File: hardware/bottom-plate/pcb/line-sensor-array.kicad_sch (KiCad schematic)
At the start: 1 part

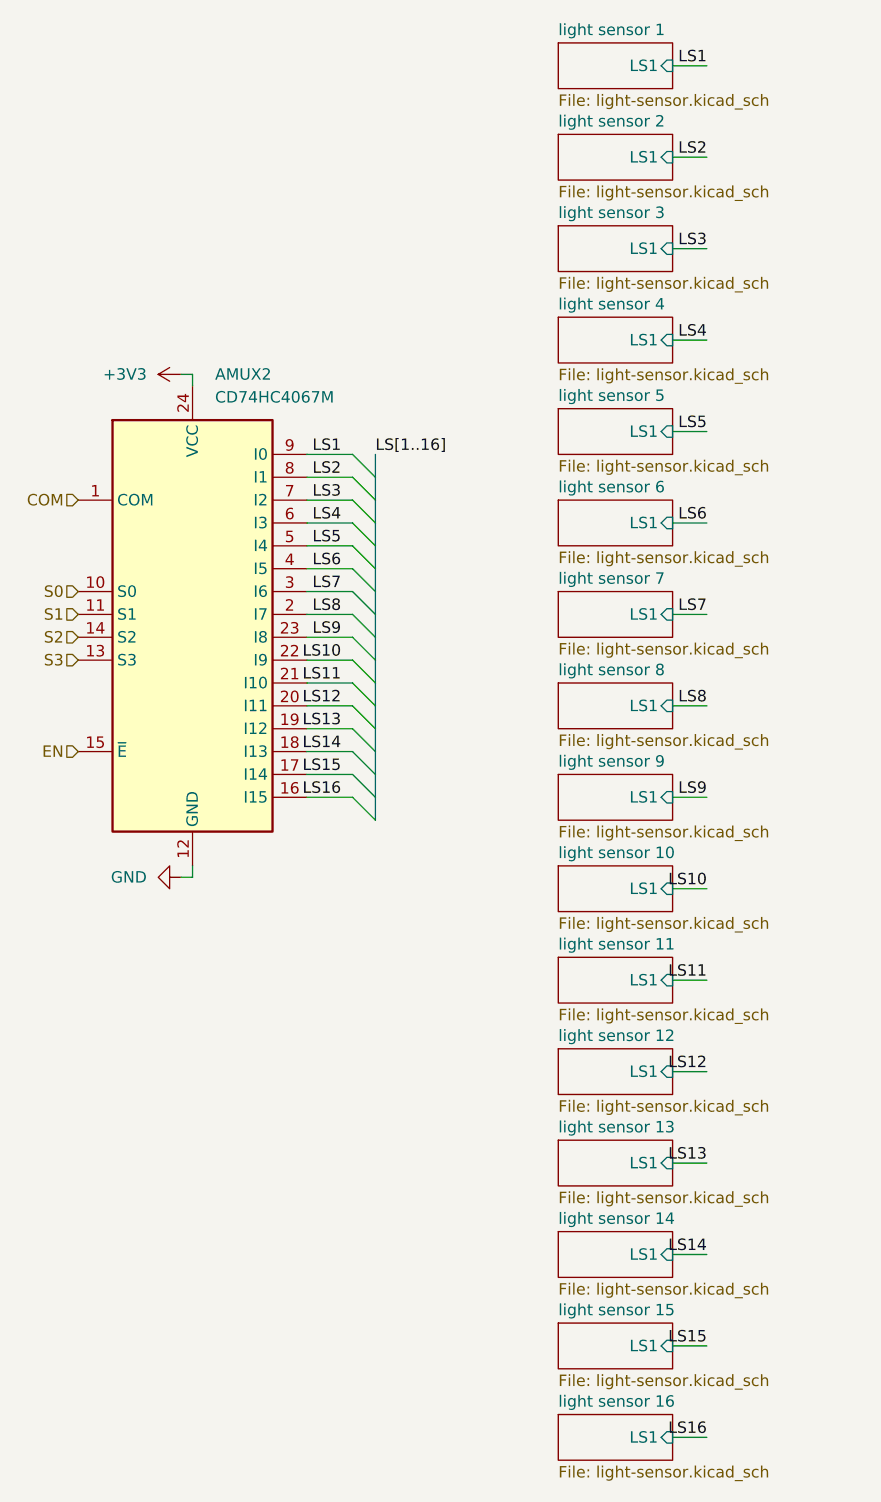
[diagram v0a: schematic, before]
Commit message: cleaned up bottom plate schematic numbering
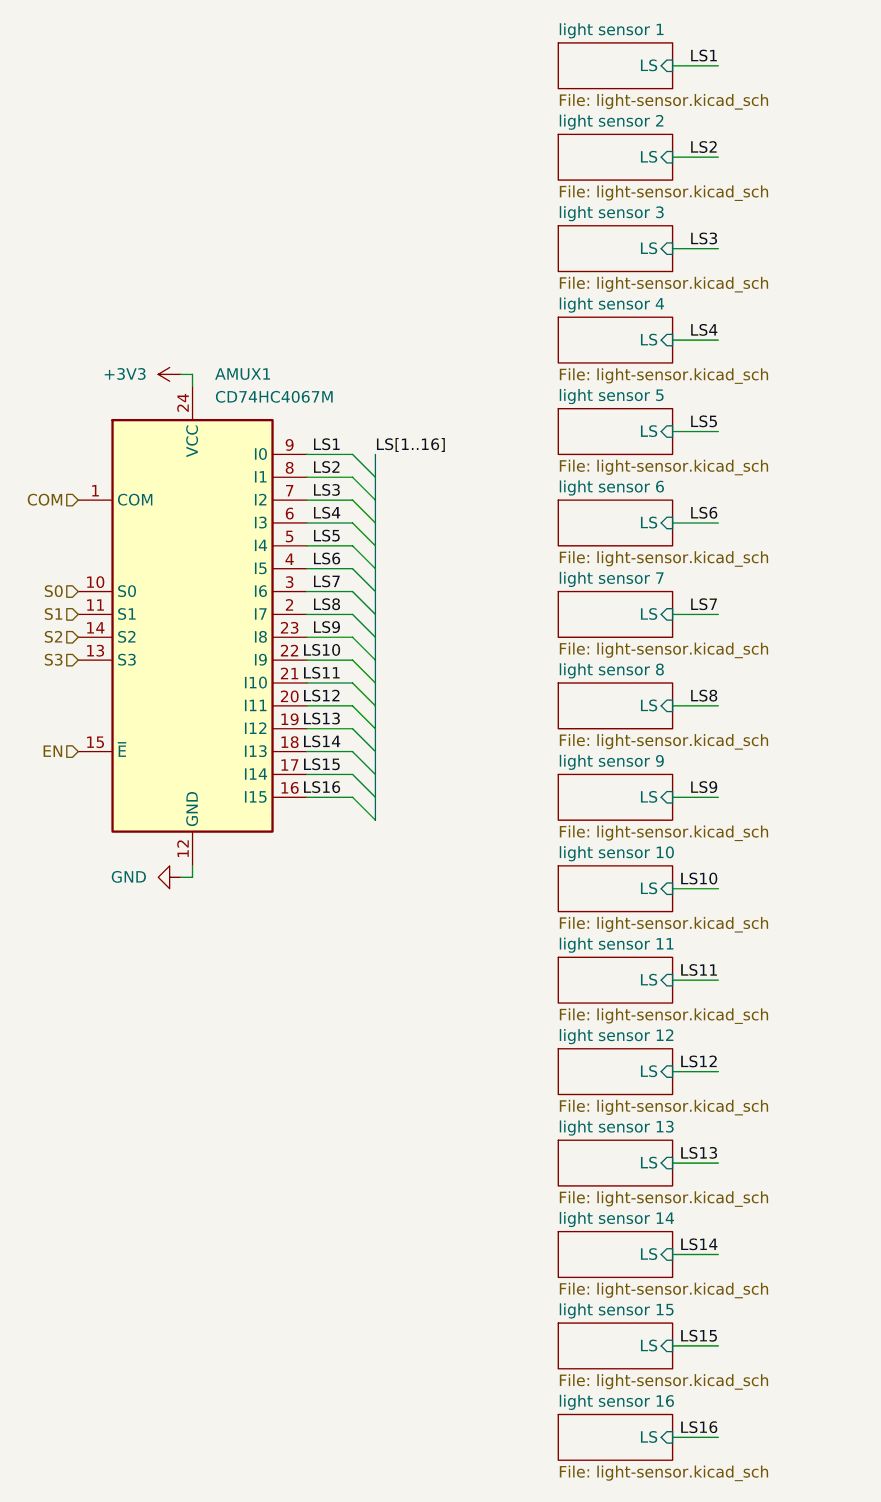
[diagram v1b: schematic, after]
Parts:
- renumbered AMUX2 to AMUX1
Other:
- sheet light sensor 1 ports: added LS; removed LS1
- sheet light sensor 10 ports: added LS; removed LS1
- sheet light sensor 11 ports: added LS; removed LS1
- sheet light sensor 12 ports: added LS; removed LS1
- sheet light sensor 13 ports: added LS; removed LS1
- sheet light sensor 14 ports: added LS; removed LS1
- sheet light sensor 15 ports: added LS; removed LS1
- sheet light sensor 16 ports: added LS; removed LS1
- sheet light sensor 2 ports: added LS; removed LS1
- sheet light sensor 3 ports: added LS; removed LS1
- sheet light sensor 4 ports: added LS; removed LS1
- sheet light sensor 5 ports: added LS; removed LS1
- sheet light sensor 6 ports: added LS; removed LS1
- sheet light sensor 7 ports: added LS; removed LS1
- sheet light sensor 8 ports: added LS; removed LS1
- sheet light sensor 9 ports: added LS; removed LS1

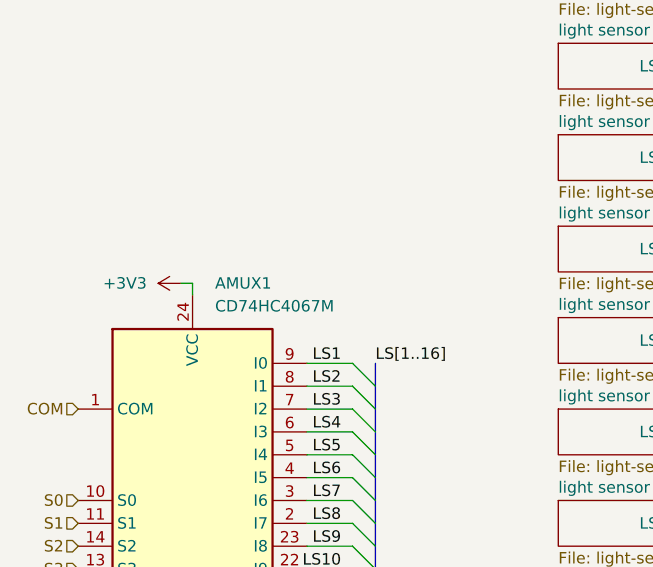
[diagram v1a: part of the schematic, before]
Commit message: fixed non convention following of kicker pcb
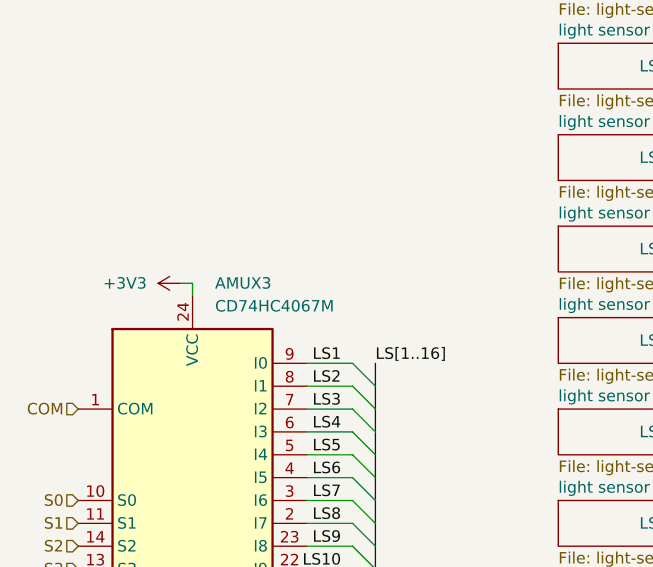
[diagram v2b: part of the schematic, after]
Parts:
- renumbered AMUX1 to AMUX3
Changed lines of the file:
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@@
 		(dnp no)
 		(fields_autoplaced yes)
-		(property "Reference" "#PWR073"
+		(property "Reference" "#PWR0211"
 			(at 81.28 63.5 0)
 			(effects
@@
 			(project "pcb"
 				(path "/7e6d4b79-c480-4b70-bccc-d28260cddf7c/93e6d7bb-95f9-4cf2-95f4-5cf0dae1bc31"
-					(reference "#PWR0205")
+					(reference "#PWR0211")
 					(unit 1)
 				)
 				(path "/7e6d4b79-c480-4b70-bccc-d28260cddf7c/c980f11d-c85b-4c7f-a7ac-bfc985564f96"
-					(reference "#PWR0139")
+					(reference "#PWR0145")
 					(unit 1)
 				)
 				(path "/7e6d4b79-c480-4b70-bccc-d28260cddf7c/dd019f33-6d81-4ff9-8ccf-108909809042"
-					(reference "#PWR073")
+					(reference "#PWR079")
 					(unit 1)
 				)
@@
 		(dnp no)
 		(fields_autoplaced yes)
-		(property "Reference" "AMUX1"
+		(property "Reference" "AMUX3"
 			(at 81.242 63.5 0)
 			(effects
@@
 		(dnp no)
 		(fields_autoplaced yes)
-		(property "Reference" "#PWR074"
+		(property "Reference" "#PWR0212"
 			(at 71.12 119.38 0)
 			(effects
@@
 			(project "pcb"
 				(path "/7e6d4b79-c480-4b70-bccc-d28260cddf7c/93e6d7bb-95f9-4cf2-95f4-5cf0dae1bc31"
-					(reference "#PWR0206")
+					(reference "#PWR0212")
 					(unit 1)
 				)
 				(path "/7e6d4b79-c480-4b70-bccc-d28260cddf7c/c980f11d-c85b-4c7f-a7ac-bfc985564f96"
-					(reference "#PWR0140")
+					(reference "#PWR0146")
 					(unit 1)
 				)
 				(path "/7e6d4b79-c480-4b70-bccc-d28260cddf7c/dd019f33-6d81-4ff9-8ccf-108909809042"
-					(reference "#PWR074")
-					(unit 1)
-				)
+					(reference "#PWR080")
+					(unit 1)
+				)
